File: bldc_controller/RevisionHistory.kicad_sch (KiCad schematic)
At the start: 0 parts

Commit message: some progress
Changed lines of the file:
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@@
     (effects (font (size 2.54 2.54) (thickness 0.508) bold (color 0 0 0 1)) (href "#1"))
   )
-  (text_box "10/12/2023: Document creation"
+  (text_box "Rev 1.0\n\n- Changed CPH-CPL capacitor to 47nF (gate driver)\n\n- Added TVS protection and termination switch to FD-CAN\n\n- Added 5V 300mA connector for external fan\n\n- Use of standard 1.27mm pitch connector for SWD\n\n- Added 2 power connectors for daisy-chain\n\n- Changed 3.3V buck converter IC"
     (at 22.86 31.75 0) (size 124.46 129.54)
     (stroke (width -0.0001) (type default))
     (fill (type none))
-    (effects (font (size 1.905 1.905) bold (color 0 0 0 1)) (justify left top))
+    (effects (font (face "Arial") (size 1.905 1.905) (color 0 0 0 1)) (justify left top))
   )
   (text_box ""

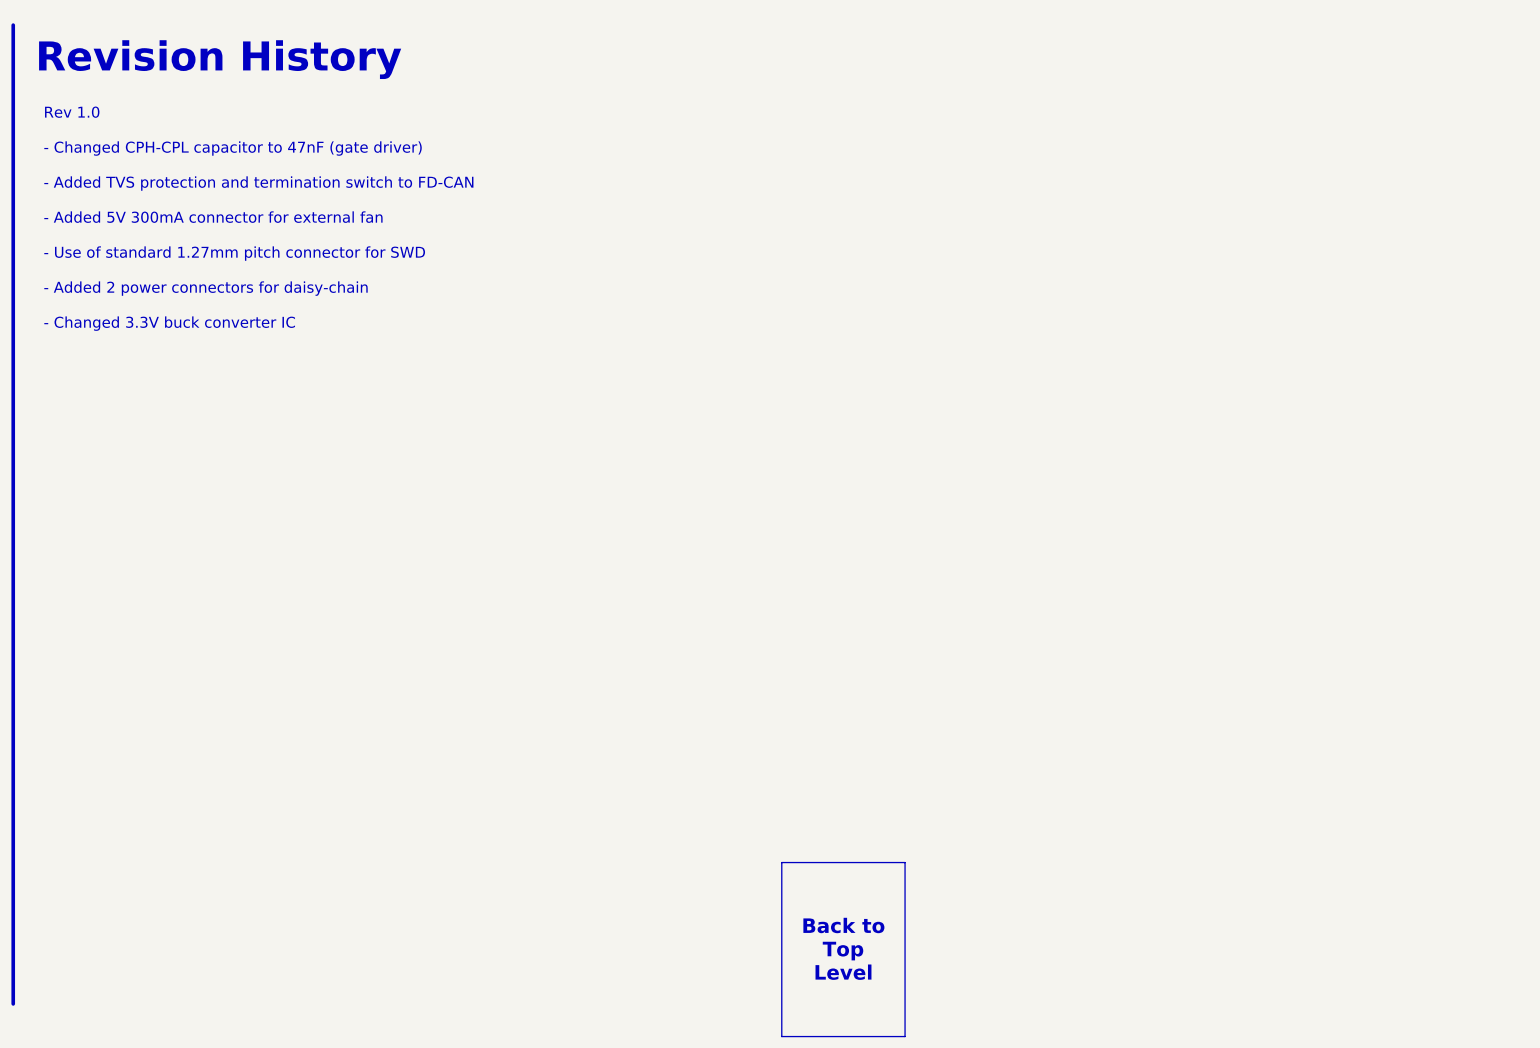
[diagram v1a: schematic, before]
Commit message: added temporary footprints and deleted extra files
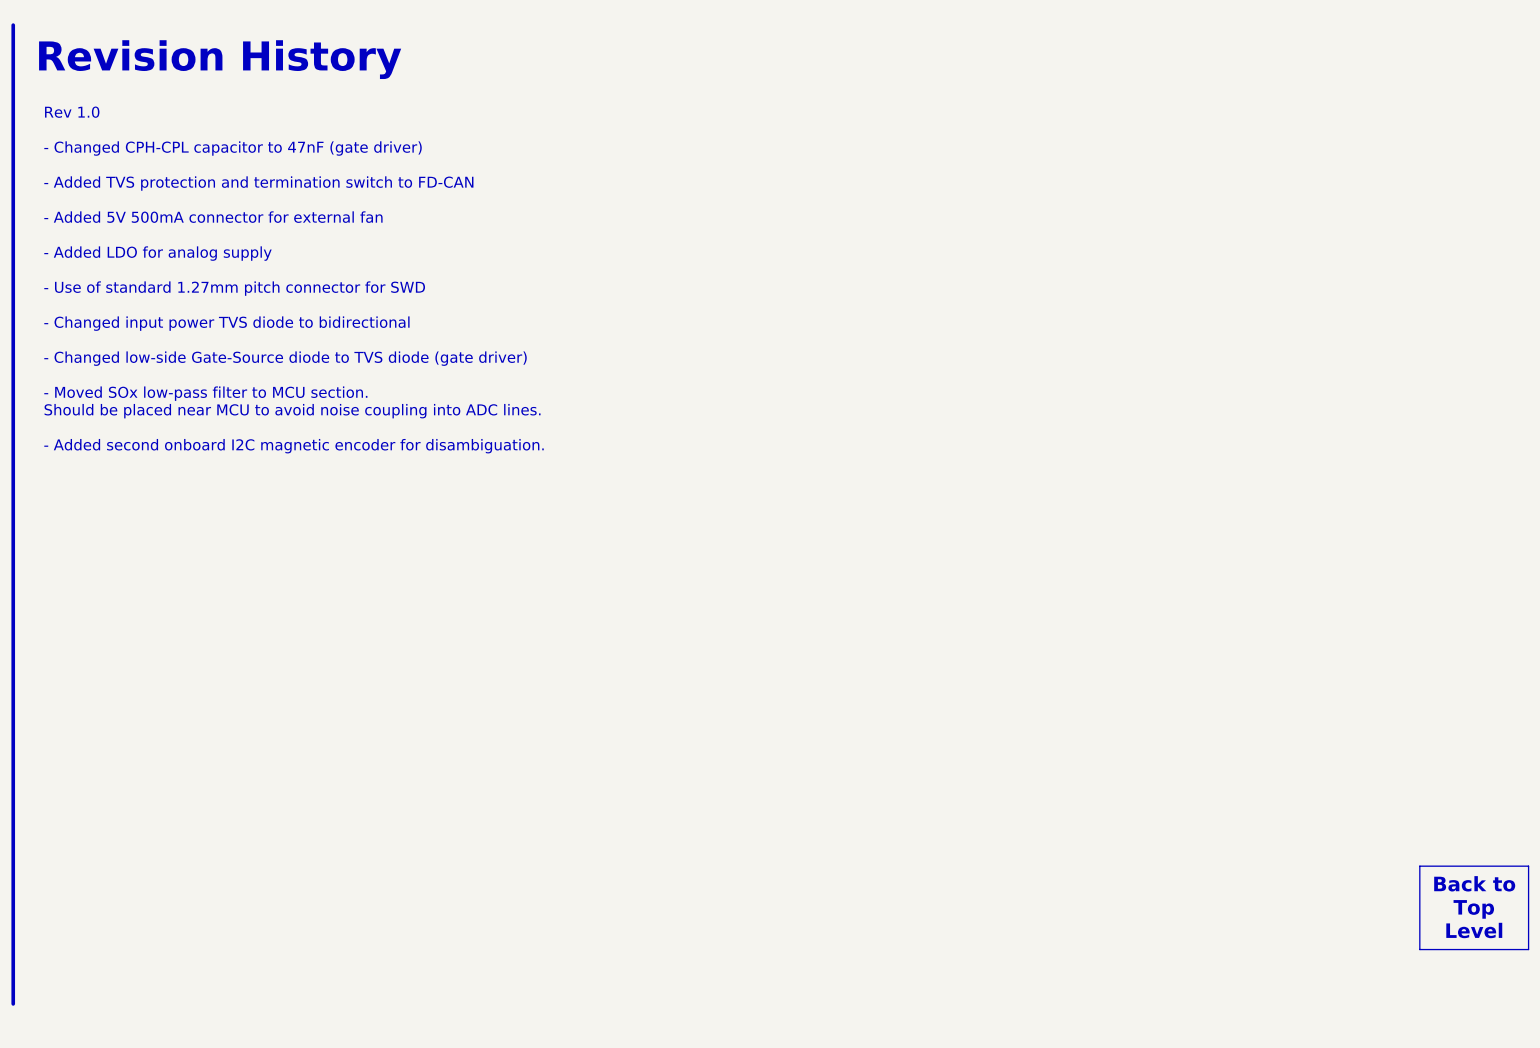
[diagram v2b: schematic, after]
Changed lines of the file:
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@@
     (stroke (width 0.635) (type default) (color 0 0 0 1))
   )
-  (text_box "Back to Top Level"
-    (at 153.67 165.735 0) (size 21.59 30.48)
-    (stroke (width 0) (type default) (color 0 0 0 1))
-    (fill (type color) (color 0 0 0 0.1))
-    (effects (font (size 2.54 2.54) (thickness 0.508) bold (color 0 0 0 1)) (href "#1"))
-  )
-  (text_box "Rev 1.0\n\n- Changed CPH-CPL capacitor to 47nF (gate driver)\n\n- Added TVS protection and termination switch to FD-CAN\n\n- Added 5V 300mA connector for external fan\n\n- Use of standard 1.27mm pitch connector for SWD\n\n- Added 2 power connectors for daisy-chain\n\n- Changed 3.3V buck converter IC"
+  (text_box "Rev 1.0\n\n- Changed CPH-CPL capacitor to 47nF (gate driver)\n\n- Added TVS protection and termination switch to FD-CAN\n\n- Added 5V 500mA connector for external fan\n\n- Added LDO for analog supply\n\n- Use of standard 1.27mm pitch connector for SWD\n\n- Changed input power TVS diode to bidirectional\n\n- Changed low-side Gate-Source diode to TVS diode (gate driver)\n\n- Moved SOx low-pass filter to MCU section. \nShould be placed near MCU to avoid noise coupling into ADC lines.\n\n- Added second onboard I2C magnetic encoder for disambiguation."
     (at 22.86 31.75 0) (size 124.46 129.54)
     (stroke (width -0.0001) (type default))
@@
     (effects (font (face "Arial") (size 1.905 1.905) (color 0 0 0 1)) (justify left top))
   )
+  (text_box "Back to Top Level"
+    (at 265.43 166.37 0) (size 19.05 14.605)
+    (stroke (width 0) (type default) (color 0 0 0 1))
+    (fill (type color) (color 0 0 0 0.1))
+    (effects (font (size 2.54 2.54) (thickness 0.508) bold (color 0 0 0 1)) (href "#1"))
+  )
   (text_box ""

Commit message: some progress on the pcb
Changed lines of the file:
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@@
     (stroke (width 0.635) (type default) (color 0 0 0 1))
   )
-  (text_box "Rev 1.0\n\n- Changed CPH-CPL capacitor to 47nF (gate driver)\n\n- Added TVS protection and termination switch to FD-CAN\n\n- Added 5V 500mA connector for external fan\n\n- Added LDO for analog supply\n\n- Use of standard 1.27mm pitch connector for SWD\n\n- Changed input power TVS diode to bidirectional\n\n- Changed low-side Gate-Source diode to TVS diode (gate driver)\n\n- Moved SOx low-pass filter to MCU section. \nShould be placed near MCU to avoid noise coupling into ADC lines.\n\n- Added second onboard I2C magnetic encoder for disambiguation."
+  (text_box "Rev 1.0\n\n- Changed CPH-CPL capacitor to 47nF (gate driver)\n\n- Added TVS protection and termination switch to FD-CAN\n\n- Added 5V 500mA connector for external fan\n\n- Added LDO for analog supply\n\n- Use of standard 1.27mm pitch connector for SWD\n\n- Changed input power TVS diode to bidirectional\n\n- Changed low-side Gate-Source diode to TVS diode (gate driver)\n\n- Moved SOx low-pass filter to MCU section. \nShould be placed near MCU to avoid noise coupling into ADC lines.\n\n- Added second onboard I2C magnetic encoder for disambiguation.\n\n- Switched PWM_PHASEA with PWM_PHASEC on STM32G474 pinout for easier routing."
     (at 22.86 31.75 0) (size 124.46 129.54)
     (stroke (width -0.0001) (type default))

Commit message: minor changes before changing mcu
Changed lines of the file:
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@@
     (stroke (width 0.635) (type default) (color 0 0 0 1))
   )
-  (text_box "Rev 1.0\n\n- Changed CPH-CPL capacitor to 47nF (gate driver)\n\n- Added TVS protection and termination switch to FD-CAN\n\n- Added 5V 500mA connector for external fan\n\n- Added LDO for analog supply\n\n- Use of standard 1.27mm pitch connector for SWD\n\n- Changed input power TVS diode to bidirectional\n\n- Changed low-side Gate-Source diode to TVS diode (gate driver)\n\n- Moved SOx low-pass filter to MCU section. \nShould be placed near MCU to avoid noise coupling into ADC lines.\n\n- Added second onboard I2C magnetic encoder for disambiguation.\n\n- Switched PWM_PHASEA with PWM_PHASEC on STM32G474 pinout for easier routing."
+  (text_box "Rev 1.0\n\n- Changed CPH-CPL capacitor to 47nF (gate driver)\n\n- Changed FD-CAN transceiver IC\n\n- Added TVS protection and termination switch to FD-CAN\n\n- Added low-side switched 12V 600mA source for external fan\n\n- Added LDO for analog supply\n\n- Changed input power TVS diode to bidirectional and added one diode per connector\n\n- Moved SOx low-pass filter to MCU section. \nShould be placed near MCU to avoid noise coupling into ADC lines.\n\n- Added second onboard I2C magnetic encoder for disambiguation.\n\n- Switched PWM_PHASEA with PWM_PHASEC on STM32G474 pinout for easier routing.\n\n- Changed RS422 pinout on connector"
     (at 22.86 31.75 0) (size 124.46 129.54)
     (stroke (width -0.0001) (type default))

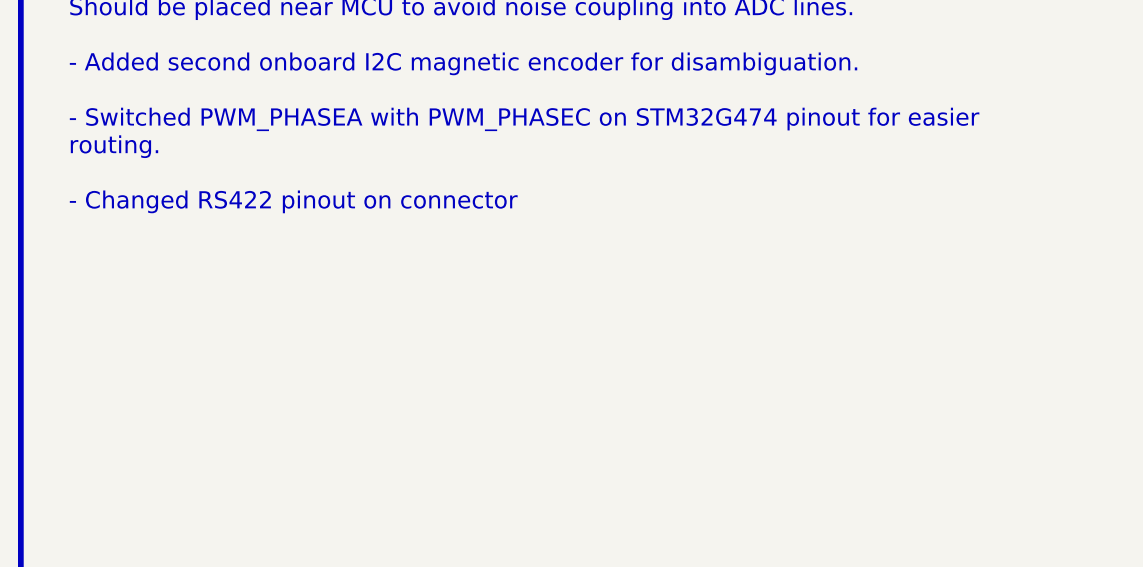
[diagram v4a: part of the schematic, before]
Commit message: Added TVS diodes to all interfaces
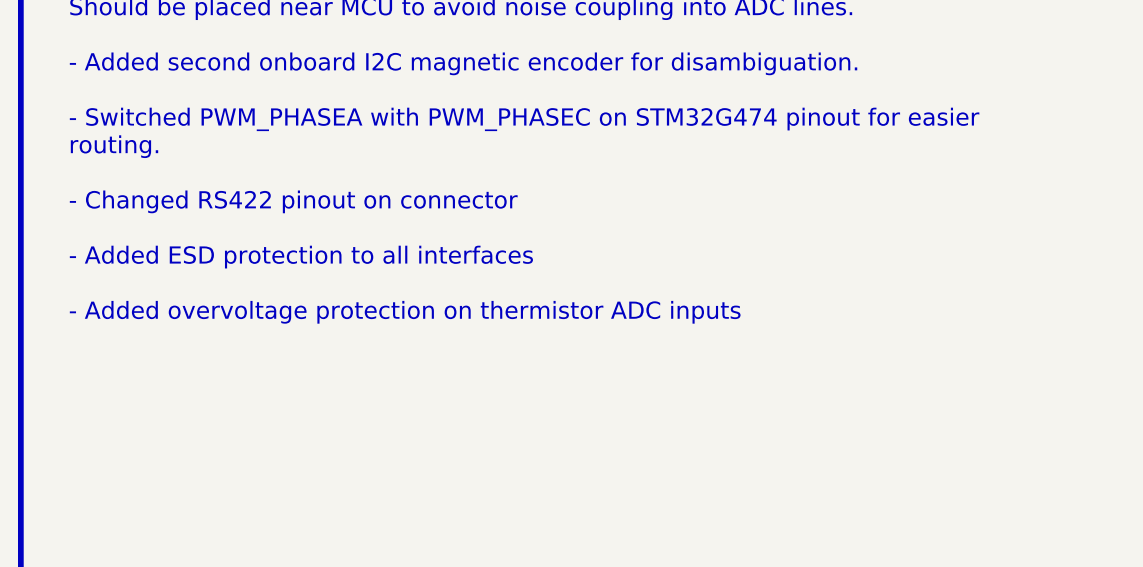
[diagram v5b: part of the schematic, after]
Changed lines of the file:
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@@
     (stroke (width 0.635) (type default) (color 0 0 0 1))
   )
-  (text_box "Rev 1.0\n\n- Changed CPH-CPL capacitor to 47nF (gate driver)\n\n- Changed FD-CAN transceiver IC\n\n- Added TVS protection and termination switch to FD-CAN\n\n- Added low-side switched 12V 600mA source for external fan\n\n- Added LDO for analog supply\n\n- Changed input power TVS diode to bidirectional and added one diode per connector\n\n- Moved SOx low-pass filter to MCU section. \nShould be placed near MCU to avoid noise coupling into ADC lines.\n\n- Added second onboard I2C magnetic encoder for disambiguation.\n\n- Switched PWM_PHASEA with PWM_PHASEC on STM32G474 pinout for easier routing.\n\n- Changed RS422 pinout on connector"
+  (text_box "Rev 1.0\n\n- Changed CPH-CPL capacitor to 47nF (gate driver)\n\n- Changed FD-CAN transceiver IC\n\n- Added TVS protection and termination switch to FD-CAN\n\n- Added low-side switched 12V 600mA source for external fan\n\n- Added LDO for analog supply\n\n- Changed input power TVS diode to bidirectional and added one diode per connector\n\n- Moved SOx low-pass filter to MCU section. \nShould be placed near MCU to avoid noise coupling into ADC lines.\n\n- Added second onboard I2C magnetic encoder for disambiguation.\n\n- Switched PWM_PHASEA with PWM_PHASEC on STM32G474 pinout for easier routing.\n\n- Changed RS422 pinout on connector\n\n- Added ESD protection to all interfaces\n\n- Added overvoltage protection on thermistor ADC inputs"
     (at 22.86 31.75 0) (size 124.46 129.54)
     (stroke (width -0.0001) (type default))

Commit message: might have fixed net issue, added dxf and svgs
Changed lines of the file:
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@@
     (comment 3 "Author: Vincent Nguyen")
   )
-  (polyline (pts (xy 19.05 19.05) (xy 19.05 190.5))
+  (polyline (pts (xy 19.05 31.75) (xy 19.05 190.5))
     (stroke (width 0.635) (type default) (color 0 0 0 1))
+  )
+  (text_box "[21] Revision History"
+    (at 80.01 16.51 0) (size 137.16 12.7)
+    (stroke (width -0.0001) (type default))
+    (fill (type none))
+    (effects (font (face "Times New Roman") (size 6 6) (thickness 1.2) bold (color 162 22 34 1)))
   )
   (text_box "Rev 1.0\n\n- Changed CPH-CPL capacitor to 47nF (gate driver)\n\n- Changed FD-CAN transceiver IC\n\n- Added TVS protection and termination switch to FD-CAN\n\n- Added low-side switched 12V 600mA source for external fan\n\n- Added LDO for analog supply\n\n- Changed input power TVS diode to bidirectional and added one diode per connector\n\n- Moved SOx low-pass filter to MCU section. \nShould be placed near MCU to avoid noise coupling into ADC lines.\n\n- Added second onboard I2C magnetic encoder for disambiguation.\n\n- Switched PWM_PHASEA with PWM_PHASEC on STM32G474 pinout for easier routing.\n\n- Changed RS422 pinout on connector\n\n- Added ESD protection to all interfaces\n\n- Added overvoltage protection on thermistor ADC inputs"
@@
     (effects (font (face "Arial") (size 1.905 1.905) (color 0 0 0 1)) (justify left top))
   )
-  (text_box "Back to Top Level"
-    (at 265.43 166.37 0) (size 19.05 14.605)
-    (stroke (width 0) (type default) (color 0 0 0 1))
-    (fill (type color) (color 0 0 0 0.1))
-    (effects (font (size 2.54 2.54) (thickness 0.508) bold (color 0 0 0 1)) (href "#1"))
-  )
   (text_box ""
     (at 152.4 31.75 0) (size 128.27 129.54)
     (stroke (width -0.0001) (type default))
     (fill (type none))
-    (effects (font (size 1.905 1.905) bold (color 0 0 0 1)) (justify left top))
-  )
-  (text_box "Revision History"
-    (at 19.05 17.78 0) (size 73.66 13.97)
-    (stroke (width -0.0001) (type default))
-    (fill (type none))
-    (effects (font (size 5.08 5.08) bold (color 0 0 0 1)) (justify left top))
+    (effects (font (face "Arial") (size 1.905 1.905) bold (color 0 0 0 1)) (justify left top))
   )
 )

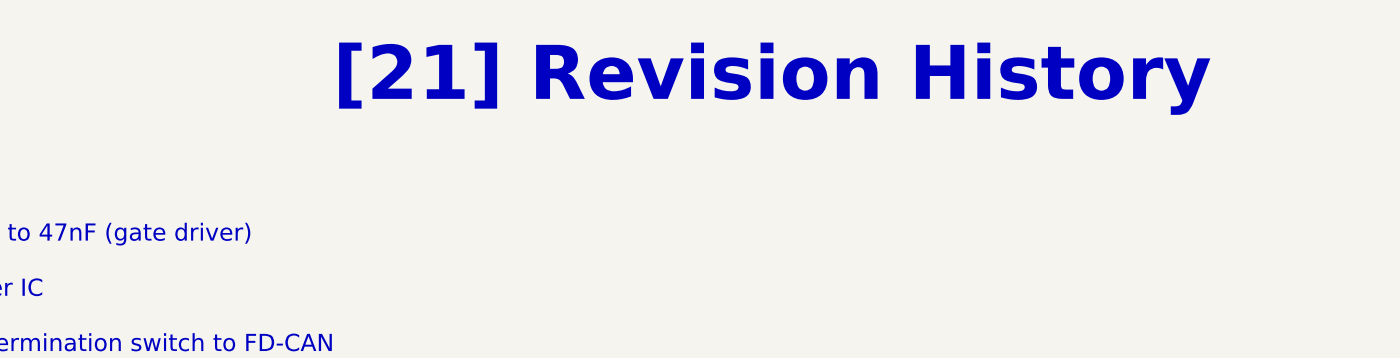
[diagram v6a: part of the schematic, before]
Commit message: Replaced 3v3 buck with WSON package alternative. Will back-annotate components
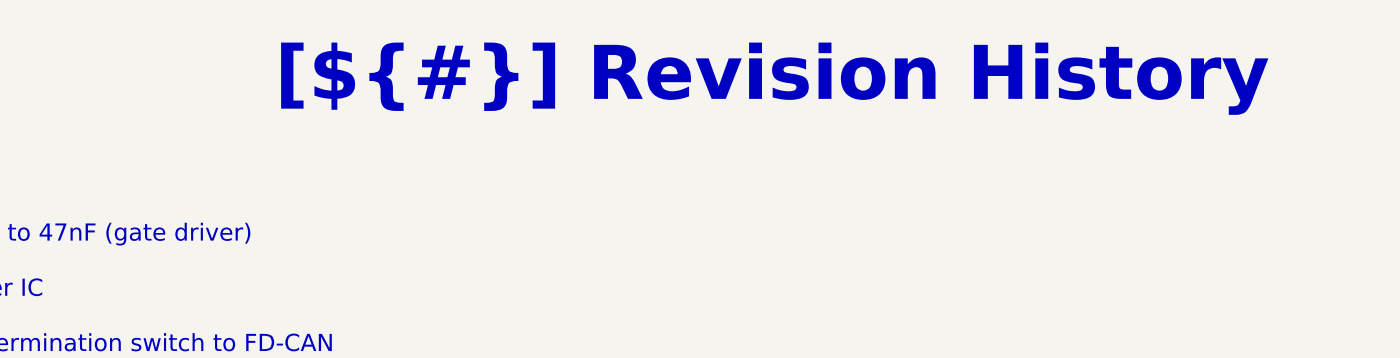
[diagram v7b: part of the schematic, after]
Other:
- company: EPFL Xplore -> ${COMPANY}
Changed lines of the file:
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@@
     (title "Revision History")
     (date "2023-10-15")
-    (rev "1.0")
-    (company "EPFL Xplore")
-    (comment 3 "Author: Vincent Nguyen")
+    (rev "${REVISION}")
+    (company "${COMPANY}")
+    (comment 3 "Author: ${AUTHOR}")
   )
   (polyline (pts (xy 19.05 31.75) (xy 19.05 190.5))
     (stroke (width 0.635) (type default) (color 0 0 0 1))
   )
-  (text_box "[21] Revision History"
+  (text_box "[${#}] ${TITLE}"
     (at 80.01 16.51 0) (size 137.16 12.7)
     (stroke (width -0.0001) (type default))
